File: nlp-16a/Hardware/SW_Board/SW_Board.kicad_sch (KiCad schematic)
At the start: 9 parts, among them J1 Conn_02x10_Odd_Even, J2 Conn_02x10_Odd_Even, J3 USB-PWR, J4 Screw_Terminal_01x02, J5 Screw_Terminal_01x02, SW1 SW_DIP_x04, SW2 SW_DIP_x08

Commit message: 見積もり他
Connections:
- net DATA0: now also J1.6 (Pin_6); no longer J1.1 (Pin_1)
- net DATA1: now also J1.8 (Pin_8); no longer J1.3 (Pin_3)
- net DATA10: now also J1.15 (Pin_15); no longer J1.6 (Pin_6)
- net DATA2: now also J1.10 (Pin_10); no longer J1.5 (Pin_5)
- net DATA3: now also J1.12 (Pin_12); no longer J1.7 (Pin_7)
- net DATA4: now also J1.14 (Pin_14); no longer J1.9 (Pin_9)
- net DATA5: now also J1.16 (Pin_16); no longer J1.11 (Pin_11)
- net DATA6: now also J1.18 (Pin_18); no longer J1.13 (Pin_13)
- net DATA7: now also J1.20 (Pin_20); no longer J1.15 (Pin_15)
- net DATA8: now also J1.19 (Pin_19); no longer J1.2 (Pin_2)
- net DATA9: now also J1.17 (Pin_17); no longer J1.4 (Pin_4)
- net VCC: now also J1.4 (Pin_4); no longer J1.17 (Pin_17)

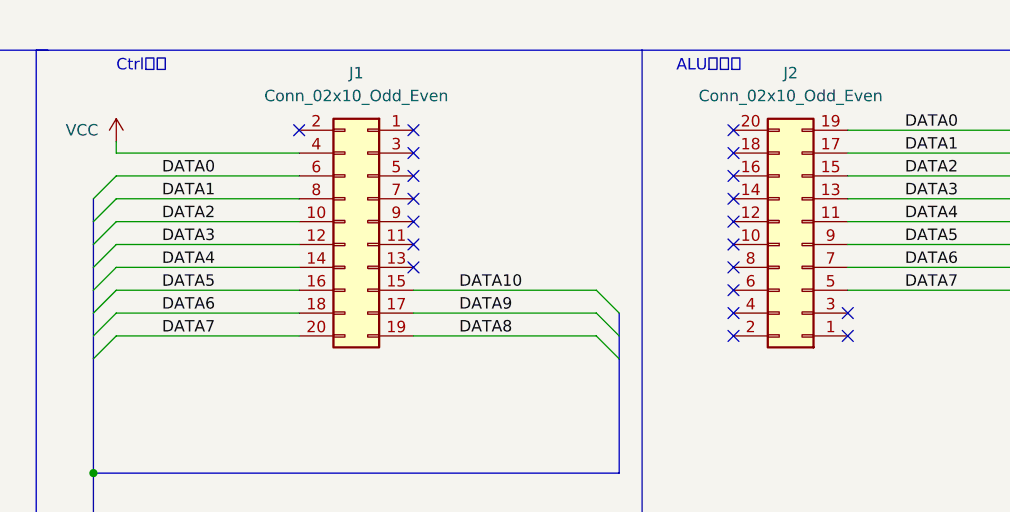
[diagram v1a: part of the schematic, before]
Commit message: ALU手動テストボード使いやすいように更新
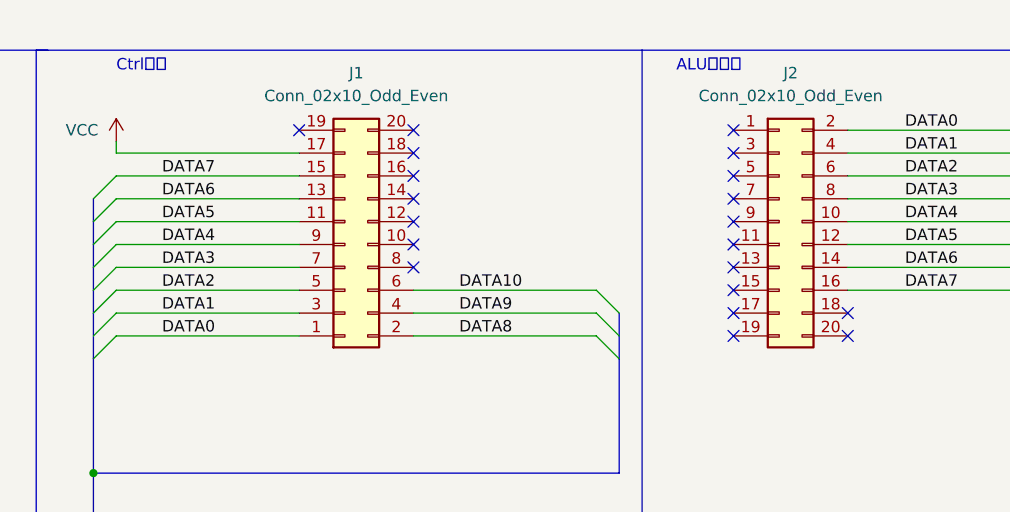
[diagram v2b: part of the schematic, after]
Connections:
- net DATA0: now also J1.1 (Pin_1), J2.2 (Pin_2); no longer J1.6 (Pin_6), J2.19 (Pin_19)
- net DATA1: now also J1.3 (Pin_3), J2.4 (Pin_4); no longer J1.8 (Pin_8), J2.17 (Pin_17)
- net DATA10: now also J1.6 (Pin_6); no longer J1.15 (Pin_15)
- net DATA2: now also J1.5 (Pin_5), J2.6 (Pin_6); no longer J1.10 (Pin_10), J2.15 (Pin_15)
- net DATA3: now also J1.7 (Pin_7), J2.8 (Pin_8); no longer J1.12 (Pin_12), J2.13 (Pin_13)
- net DATA4: now also J1.9 (Pin_9), J2.10 (Pin_10); no longer J1.14 (Pin_14), J2.11 (Pin_11)
- net DATA5: now also J1.11 (Pin_11), J2.12 (Pin_12); no longer J1.16 (Pin_16), J2.9 (Pin_9)
- net DATA6: now also J1.13 (Pin_13), J2.14 (Pin_14); no longer J1.18 (Pin_18), J2.7 (Pin_7)
- net DATA7: now also J1.15 (Pin_15), J2.16 (Pin_16); no longer J1.20 (Pin_20), J2.5 (Pin_5)
- net DATA8: now also J1.2 (Pin_2); no longer J1.19 (Pin_19)
- net DATA9: now also J1.4 (Pin_4); no longer J1.17 (Pin_17)
- net VCC: now also J1.17 (Pin_17); no longer J1.4 (Pin_4)
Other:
- moved on the sheet: J2
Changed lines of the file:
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@@
     (effects (font (size 1.27 1.27)) (justify left bottom))
   )
-  (label "DATA2" (at 104.14 46.99 0)
+  (label "DATA2" (at 104.14 54.61 0)
     (effects (font (size 1.27 1.27)) (justify left bottom))
   )
@@
     (effects (font (size 1.27 1.27)) (justify left bottom))
   )
-  (label "DATA1" (at 104.14 44.45 0)
+  (label "DATA1" (at 104.14 57.15 0)
     (effects (font (size 1.27 1.27)) (justify left bottom))
   )
@@
     (effects (font (size 1.27 1.27)) (justify left bottom))
   )
-  (label "DATA7" (at 104.14 59.69 0)
-    (effects (font (size 1.27 1.27)) (justify left bottom))
-  )
-  (label "DATA6" (at 104.14 57.15 0)
+  (label "DATA7" (at 104.14 41.91 0)
+    (effects (font (size 1.27 1.27)) (justify left bottom))
+  )
+  (label "DATA6" (at 104.14 44.45 0)
     (effects (font (size 1.27 1.27)) (justify left bottom))
   )
@@
     (effects (font (size 1.27 1.27)) (justify left bottom))
   )
-  (label "DATA4" (at 104.14 52.07 0)
+  (label "DATA4" (at 104.14 49.53 0)
     (effects (font (size 1.27 1.27)) (justify left bottom))
   )
@@
     (effects (font (size 1.27 1.27)) (justify left bottom))
   )
-  (label "DATA0" (at 104.14 41.91 0)
+  (label "DATA0" (at 104.14 59.69 0)
     (effects (font (size 1.27 1.27)) (justify left bottom))
   )
@@
     (effects (font (size 1.27 1.27)) (justify left bottom))
   )
-  (label "DATA5" (at 104.14 54.61 0)
+  (label "DATA5" (at 104.14 46.99 0)
     (effects (font (size 1.27 1.27)) (justify left bottom))
   )
@@
     (effects (font (size 1.27 1.27)) (justify left bottom))
   )
-  (label "DATA3" (at 104.14 49.53 0)
+  (label "DATA3" (at 104.14 52.07 0)
     (effects (font (size 1.27 1.27)) (justify left bottom))
   )
@@
     (pin "5")
   )
-  (symbol (lib_id "Connector_Generic:Conn_02x10_Odd_Even") (at 127 46.99 0) (mirror y) (unit 1)
+  (symbol (lib_id "Connector_Generic:Conn_02x10_Odd_Even") (at 124.46 49.53 0) (mirror x) (unit 1)
     (in_bom yes) (on_board yes) (fields_autoplaced)
     (property "Reference" "J1" (id 0) (at 125.73 30.48 0))
     (property "Value" "Conn_02x10_Odd_Even" (id 1) (at 125.73 33.02 0))
-    (property "Footprint" "Connector_PinHeader_2.54mm:PinHeader_2x10_P2.54mm_Vertical" (id 2) (at 127 46.99 0)
-      (effects (font (size 1.27 1.27)) hide)
-    )
-    (property "Datasheet" "~" (id 3) (at 127 46.99 0)
+    (property "Footprint" "Connector_PinHeader_2.54mm:PinHeader_2x10_P2.54mm_Vertical" (id 2) (at 124.46 49.53 0)
+      (effects (font (size 1.27 1.27)) hide)
+    )
+    (property "Datasheet" "~" (id 3) (at 124.46 49.53 0)
       (effects (font (size 1.27 1.27)) hide)
     )
@@
     (pin "1")
   )
-  (symbol (lib_id "Connector_Generic:Conn_02x10_Odd_Even") (at 175.26 49.53 180) (unit 1)
+  (symbol (lib_id "Connector_Generic:Conn_02x10_Odd_Even") (at 172.72 46.99 0) (unit 1)
     (in_bom yes) (on_board yes) (fields_autoplaced)
     (property "Reference" "J2" (id 0) (at 173.99 30.48 0))
     (property "Value" "Conn_02x10_Odd_Even" (id 1) (at 173.99 33.02 0))
-    (property "Footprint" "Connector_PinHeader_2.54mm:PinHeader_2x10_P2.54mm_Vertical" (id 2) (at 175.26 49.53 0)
-      (effects (font (size 1.27 1.27)) hide)
-    )
-    (property "Datasheet" "~" (id 3) (at 175.26 49.53 0)
-      (effects (font (size 1.27 1.27)) hide)
-    )
+    (property "Footprint" "Connector_PinHeader_2.54mm:PinHeader_2x10_P2.54mm_Vertical" (id 2) (at 172.72 46.99 0)
+      (effects (font (size 1.27 1.27)) hide)
+    )
+    (property "Datasheet" "~" (id 3) (at 172.72 46.99 0)
+      (effects (font (size 1.27 1.27)) hide)
+    )
